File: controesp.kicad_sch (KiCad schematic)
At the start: 10 parts, among them J14 Conn_01x16_Socket, J2 Screw_Terminal_01x04, J3 Conn_01x14_Socket, J4 Conn_01x14_Pin, J5 Conn_01x16_Pin, J8 Screw_Terminal_01x04, U1 N7805-1PV

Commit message: pcb layout finished
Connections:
- net controesp_hat/25: now also J5.4 (Pin_4)
- net controesp_hat/26: now also J5.5 (Pin_5)
- net controesp_hat/GND: no longer J4.13 (Pin_13), J4.14 (Pin_14)
- net input/DI1: now also J14.5 (Pin_5); no longer J14.1 (Pin_1)
- net input/DI2: now also J14.6 (Pin_6); no longer J14.2 (Pin_2)
- net input/DI3: now also J14.7 (Pin_7); no longer J14.5 (Pin_5)
- net input/DI4: now also J14.8 (Pin_8); no longer J14.6 (Pin_6)
- net input/DI5: now also J14.1 (Pin_1); no longer J14.7 (Pin_7)
- net input/DI6: now also J14.2 (Pin_2); no longer J14.8 (Pin_8)
- net input/DI7: now also J14.3 (Pin_3); no longer J14.4 (Pin_4)
- net input/DI8: now also J14.4 (Pin_4); no longer J14.3 (Pin_3)
- net powerOutput/DO13: now reaches J3.13 (Pin_13)
- net powerOutput/DO14: now reaches J3.14 (Pin_14)
- new net controesp_hat/P14: J4.13 (Pin_13)
- new net controesp_hat/P15: J4.14 (Pin_14)
- no-connect marks 2 -> 0
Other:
- sheet controesp_hat ports: added P14, P15; removed none
- sheet powerOutput ports: added DO13, DO14; removed none
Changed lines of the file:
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@@
 	)
 	(junction
-		(at 182.88 87.63)
-		(diameter 0)
-		(color 0 0 0 0)
-	)
-	(junction
 		(at 26.67 24.13)
 		(diameter 0)
@@
 		(color 0 0 0 0)
 	)
-	(no_connect
-		(at 195.58 85.09)
-	)
-	(no_connect
-		(at 195.58 87.63)
-	)
 	(wire
 		(pts
@@
 	(wire
 		(pts
+			(xy 195.58 87.63) (xy 207.01 87.63)
+		)
+		(stroke
+			(width 0)
+			(type default)
+		)
+	)
+	(wire
+		(pts
 			(xy 153.67 92.71) (xy 154.94 92.71)
 		)
@@
 	(wire
 		(pts
-			(xy 43.18 80.01) (xy 46.99 80.01)
+			(xy 195.58 85.09) (xy 207.01 85.09)
 		)
 		(stroke
@@
 	(wire
 		(pts
-			(xy 44.45 58.42) (xy 60.96 58.42)
+			(xy 43.18 80.01) (xy 46.99 80.01)
 		)
 		(stroke
@@
 	(wire
 		(pts
-			(xy 43.18 82.55) (xy 46.99 82.55)
+			(xy 44.45 58.42) (xy 60.96 58.42)
 		)
 		(stroke
@@
 	(wire
 		(pts
-			(xy 152.4 54.61) (xy 154.94 54.61)
+			(xy 43.18 82.55) (xy 46.99 82.55)
 		)
 		(stroke
@@
 	(wire
 		(pts
-			(xy 179.07 69.85) (xy 182.88 69.85)
+			(xy 152.4 54.61) (xy 154.94 54.61)
 		)
 		(stroke
@@
 	(wire
 		(pts
-			(xy 152.4 82.55) (xy 153.67 82.55)
+			(xy 179.07 69.85) (xy 182.88 69.85)
 		)
 		(stroke
@@
 	(wire
 		(pts
-			(xy 41.91 33.02) (xy 41.91 31.75)
+			(xy 152.4 82.55) (xy 153.67 82.55)
 		)
 		(stroke
@@
 	(wire
 		(pts
-			(xy 182.88 99.06) (xy 182.88 87.63)
+			(xy 41.91 33.02) (xy 41.91 31.75)
 		)
 		(stroke
@@
 	(wire
 		(pts
-			(xy 95.25 85.09) (xy 99.06 85.09)
+			(xy 179.07 85.09) (xy 182.88 85.09)
 		)
 		(stroke
@@
 	(wire
 		(pts
-			(xy 26.67 31.75) (xy 41.91 31.75)
+			(xy 95.25 85.09) (xy 99.06 85.09)
 		)
 		(stroke
@@
 	(wire
 		(pts
-			(xy 119.38 77.47) (xy 139.7 77.47)
+			(xy 26.67 31.75) (xy 41.91 31.75)
 		)
 		(stroke
@@
 	(wire
 		(pts
-			(xy 95.25 88.9) (xy 95.25 87.63)
+			(xy 119.38 77.47) (xy 139.7 77.47)
 		)
 		(stroke
@@
 	(wire
 		(pts
-			(xy 179.07 57.15) (xy 182.88 57.15)
+			(xy 95.25 88.9) (xy 95.25 87.63)
 		)
 		(stroke
@@
 	(wire
 		(pts
-			(xy 153.67 92.71) (xy 153.67 99.06)
+			(xy 179.07 57.15) (xy 182.88 57.15)
 		)
 		(stroke
@@
 	(wire
 		(pts
-			(xy 203.2 92.71) (xy 203.2 88.9)
+			(xy 203.2 92.71) (xy 203.2 90.17)
 		)
 		(stroke
@@
 	(wire
 		(pts
-			(xy 153.67 99.06) (xy 182.88 99.06)
+			(xy 195.58 59.69) (xy 207.01 59.69)
 		)
 		(stroke
@@
 	(wire
 		(pts
-			(xy 195.58 59.69) (xy 207.01 59.69)
+			(xy 195.58 74.93) (xy 207.01 74.93)
 		)
 		(stroke
@@
 	(wire
 		(pts
-			(xy 195.58 74.93) (xy 207.01 74.93)
+			(xy 179.07 72.39) (xy 182.88 72.39)
 		)
 		(stroke
@@
 	(wire
 		(pts
-			(xy 179.07 72.39) (xy 182.88 72.39)
+			(xy 179.07 87.63) (xy 182.88 87.63)
 		)
 		(stroke
@@
 	(wire
 		(pts
-			(xy 203.2 88.9) (xy 207.01 88.9)
+			(xy 203.2 90.17) (xy 207.01 90.17)
 		)
 		(stroke
@@
 	(wire
 		(pts
-			(xy 182.88 85.09) (xy 182.88 87.63)
-		)
-		(stroke
-			(width 0)
-			(type default)
-		)
-	)
-	(wire
-		(pts
 			(xy 152.4 87.63) (xy 154.94 87.63)
 		)
@@
 		)
 		(pin "DI1" input
-			(at 119.38 54.61 0)
+			(at 119.38 64.77 0)
 			(effects
 				(font
@@
 		)
 		(pin "DI2" input
-			(at 119.38 57.15 0)
+			(at 119.38 67.31 0)
 			(effects
 				(font
@@
 		)
 		(pin "DI3" input
-			(at 119.38 64.77 0)
+			(at 119.38 69.85 0)
 			(effects
 				(font
@@
 		)
 		(pin "DI4" input
-			(at 119.38 67.31 0)
+			(at 119.38 72.39 0)
 			(effects
 				(font
@@
 		)
 		(pin "DI5" input
-			(at 119.38 69.85 0)
+			(at 119.38 54.61 0)
 			(effects
 				(font
@@
 		)
 		(pin "DI6" input
-			(at 119.38 72.39 0)
+			(at 119.38 57.15 0)
 			(effects
 				(font
@@
 		)
 		(pin "DI7" input
-			(at 119.38 62.23 0)
+			(at 119.38 59.69 0)
 			(effects
 				(font
@@
 		)
 		(pin "DI8" input
-			(at 119.38 59.69 0)
+			(at 119.38 62.23 0)
 			(effects
 				(font
@@
 		)
 		(pin "GND" input
-			(at 207.01 88.9 180)
+			(at 207.01 90.17 180)
+			(effects
+				(font
+					(size 1.27 1.27)
+				)
+				(justify left)
+			)
+		)
+		(pin "DO13" input
+			(at 207.01 85.09 180)
+			(effects
+				(font
+					(size 1.27 1.27)
+				)
+				(justify left)
+			)
+		)
+		(pin "DO14" input
+			(at 207.01 87.63 180)
 			(effects
 				(font
@@
 		)
 		(pin "25" input
-			(at 166.37 50.8 90)
+			(at 154.94 62.23 180)
 			(effects
 				(font
 					(size 1.27 1.27)
 				)
-				(justify right)
+				(justify left)
 			)
 		)
 		(pin "26" input
-			(at 168.91 50.8 90)
+			(at 154.94 64.77 180)
 			(effects
 				(font
 					(size 1.27 1.27)
 				)
-				(justify right)
+				(justify left)
 			)
 		)
@@
 			)
 		)
+		(pin "P14" input
+			(at 179.07 85.09 0)
+			(effects
+				(font
+					(size 1.27 1.27)
+				)
+				(justify right)
+			)
+		)
+		(pin "P15" input
+			(at 179.07 87.63 0)
+			(effects
+				(font
+					(size 1.27 1.27)
+				)
+				(justify right)
+			)
+		)

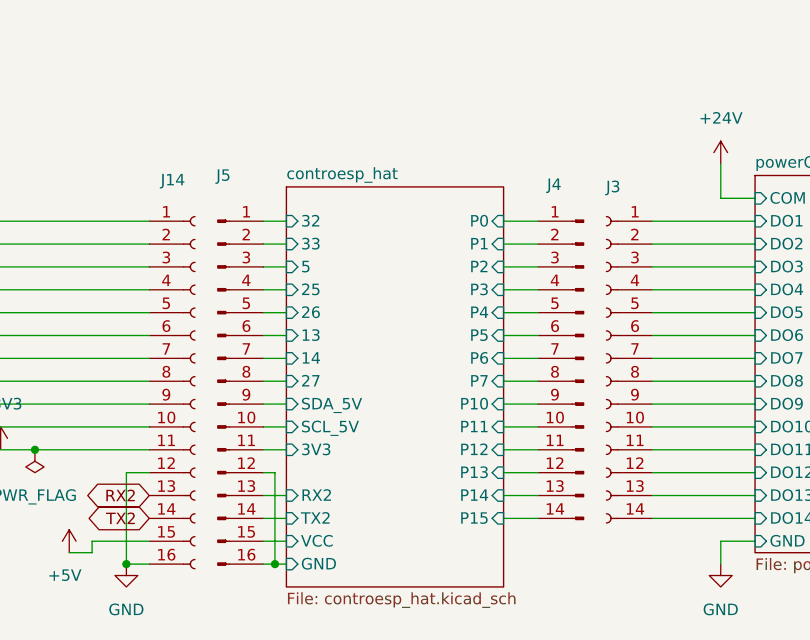
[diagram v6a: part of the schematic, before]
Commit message: splitted hat pcb into seperate proj
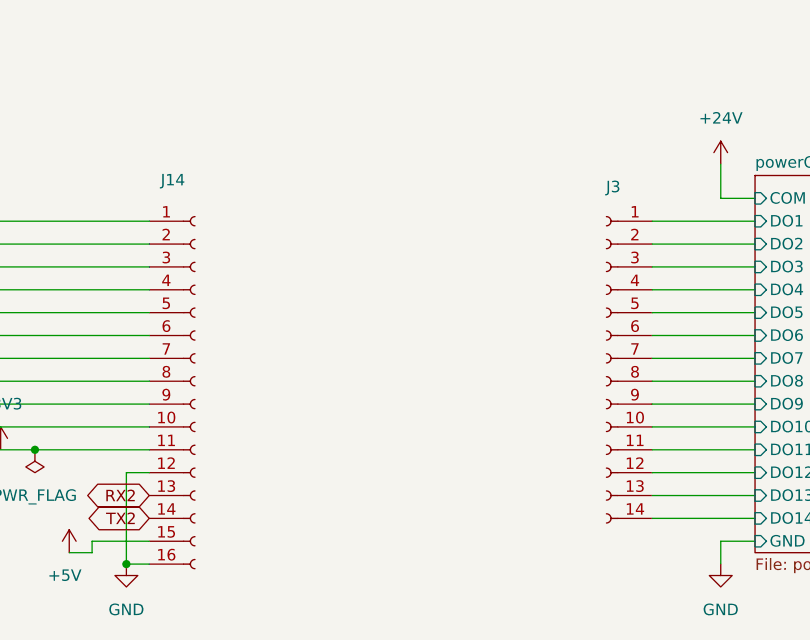
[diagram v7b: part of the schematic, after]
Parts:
- removed J4: Conn_01x14_Pin, Connector_PinHeader_2.54mm:PinHeader_1x14_P2.54mm_Vertical, symbol Connector:Conn_01x14_Pin
- removed J5: Conn_01x16_Pin, Connector_PinHeader_2.54mm:PinHeader_1x16_P2.54mm_Vertical, symbol Connector:Conn_01x16_Pin
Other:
- removed sheet controesp_hat
